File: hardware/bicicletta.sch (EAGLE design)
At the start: 2 parts

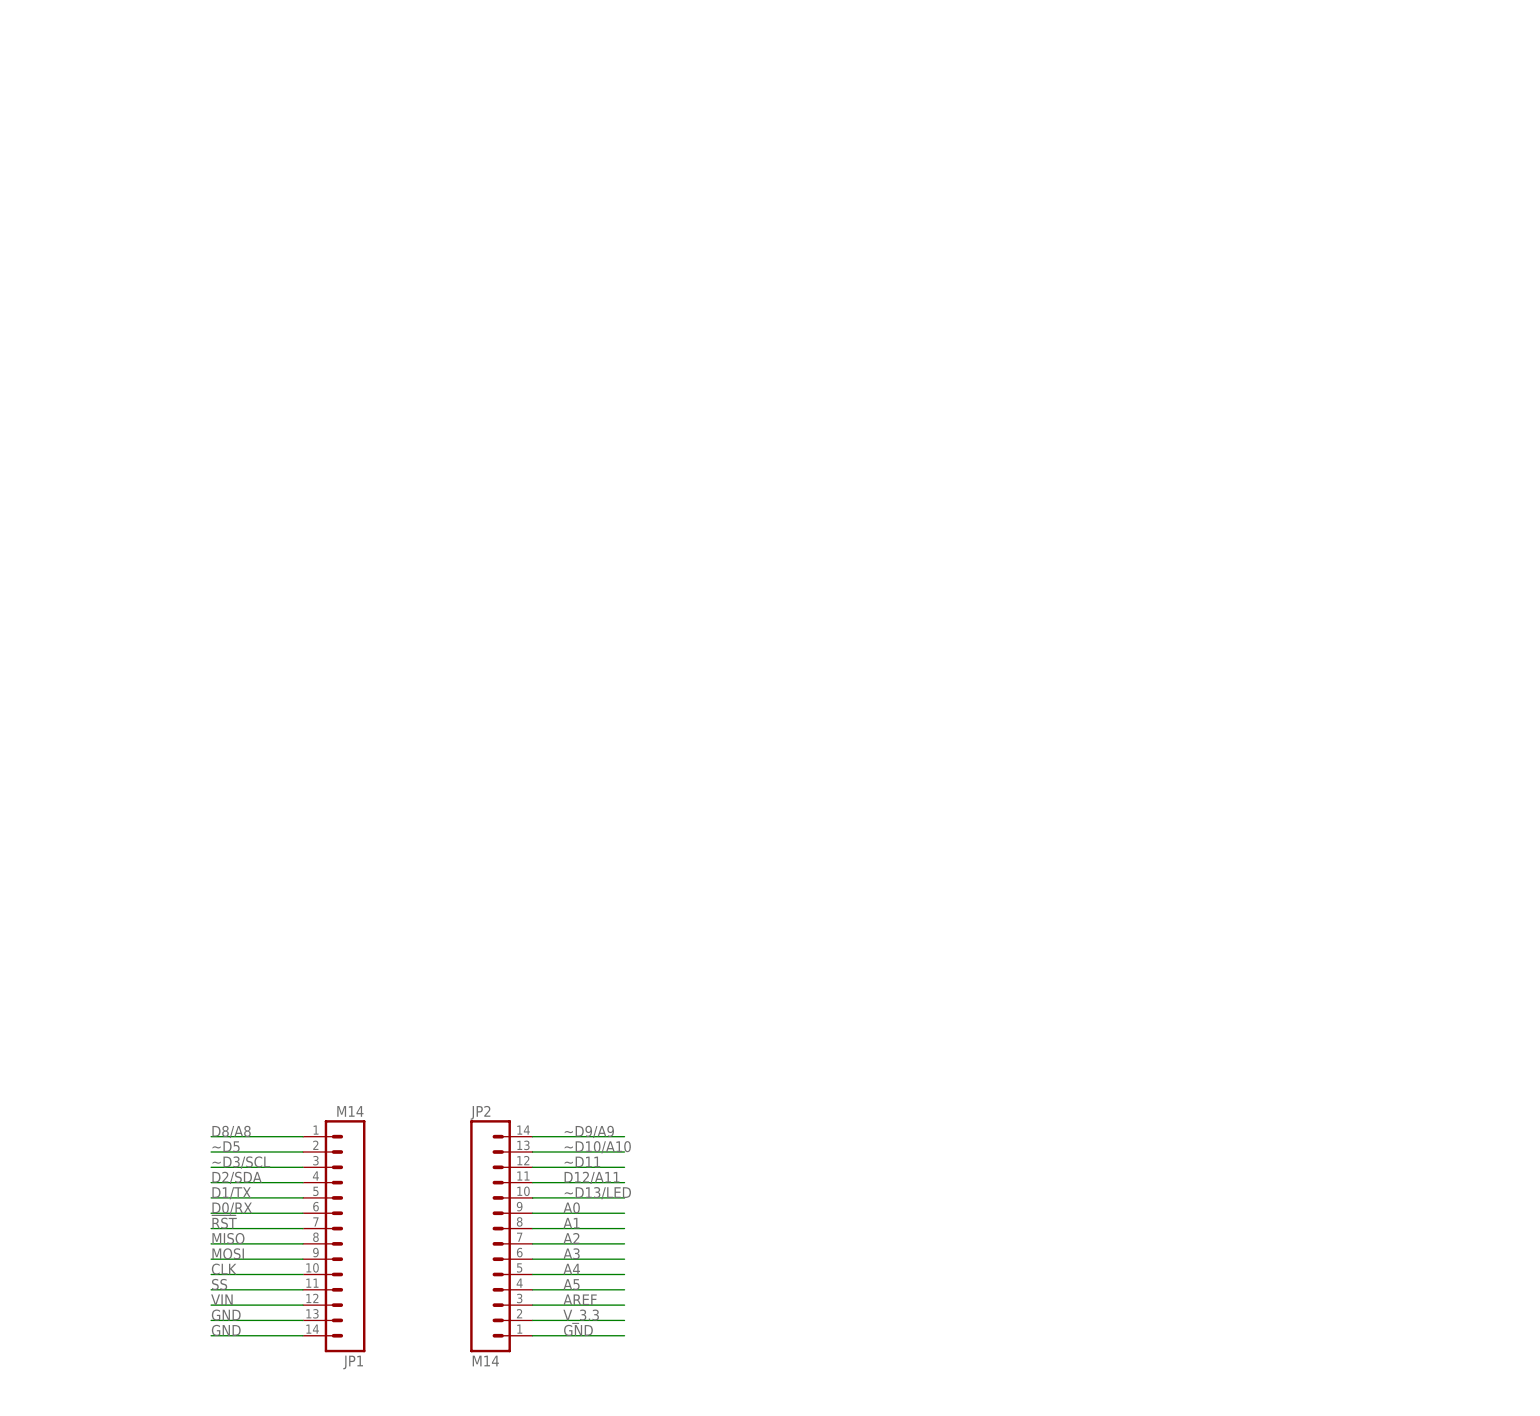
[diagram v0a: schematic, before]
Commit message: Switching regulator is set up in schematic.
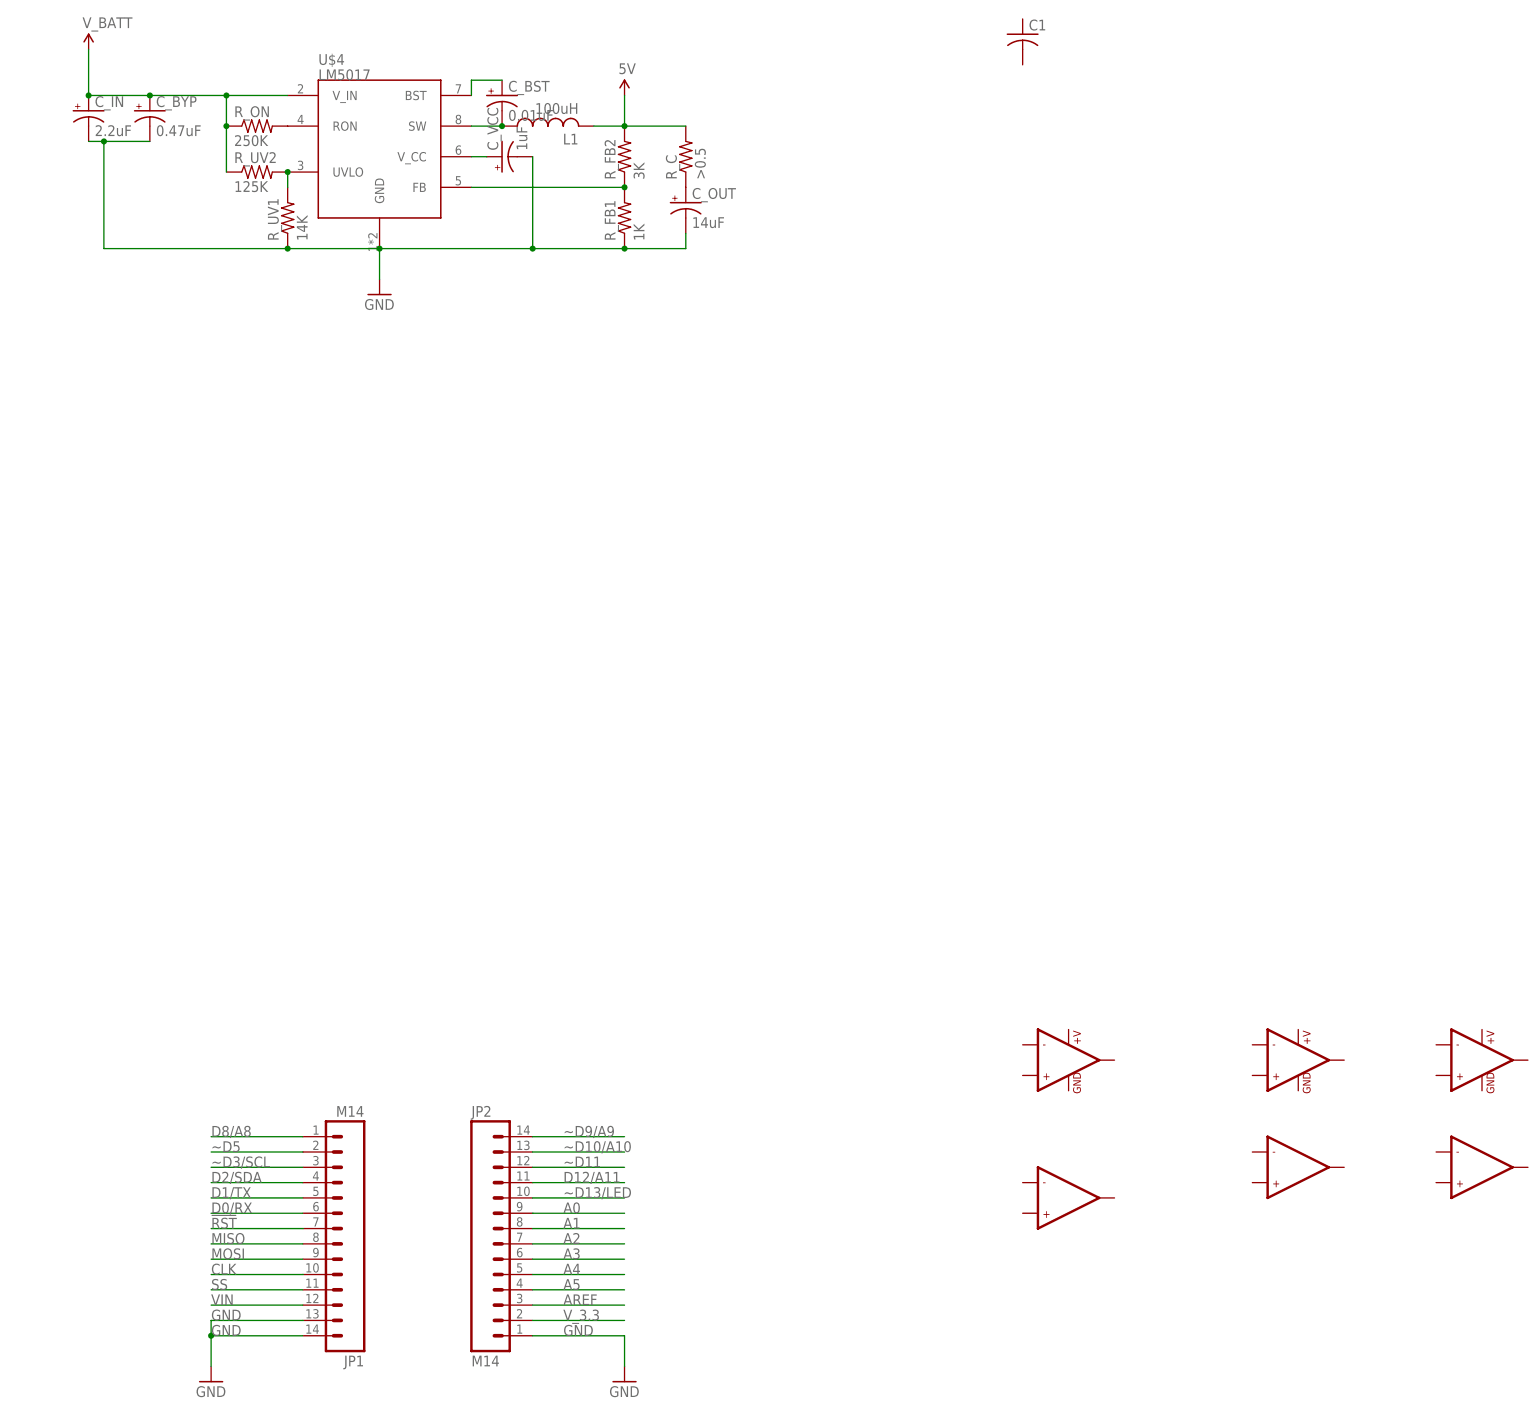
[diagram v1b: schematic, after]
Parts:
- added C1: (no value), rcl:C-USC0805
- added C_BST: 0.01uF, rcl:CPOL-USUD-5X5,8
- added C_BYP: 0.47uF, rcl:CPOL-USUD-5X5,8
- added C_IN: 2.2uF, rcl:CPOL-USUD-5X5,8
- added C_OUT: 14uF, rcl:CPOL-USUD-5X5,8
- added C_VCC: 1uF, rcl:CPOL-USUD-5X5,8
- added L1: 100uH, rcl:L-USL1812
- added R_C: >0.5, rcl:R-US_M0805
- added R_FB1: 1K, rcl:R-US_M0805
- added R_FB2: 3K, rcl:R-US_M0805
- added R_ON: 250K, rcl:R-US_M0805
- added R_UV1: 14K, rcl:R-US_M0805
- added R_UV2: 125K, rcl:R-US_M0805
- added U$1, U$2, U$3: LMV358, SparkFun-AnalogIC:LMV358
- added U$4: LM5017, Railstars:LM5017
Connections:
- new net 1.8V: C_BYP.+, C_IN.+, R_ON.1, R_UV2.1, U$4.V_IN
- new net 5V: L1.2, R_C.2, R_FB2.2
- new net N$1: R_ON.2, U$4.RON
- new net N$2: R_FB1.2, R_FB2.1, U$4.FB
- new net N$3: R_UV1.2, R_UV2.2, U$4.UVLO
- new net N$4: C_VCC.+, U$4.V_CC
- new net N$5: C_BST.-, L1.1, U$4.SW
- new net N$6: C_BST.+, U$4.BST
- new net N$7: C_OUT.+, R_C.1
- net GND: now also C_BYP.-, C_IN.-, C_OUT.-, C_VCC.-, R_FB1.1, R_UV1.1, U$4.GND

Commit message: Added 3.3V LDO regulator
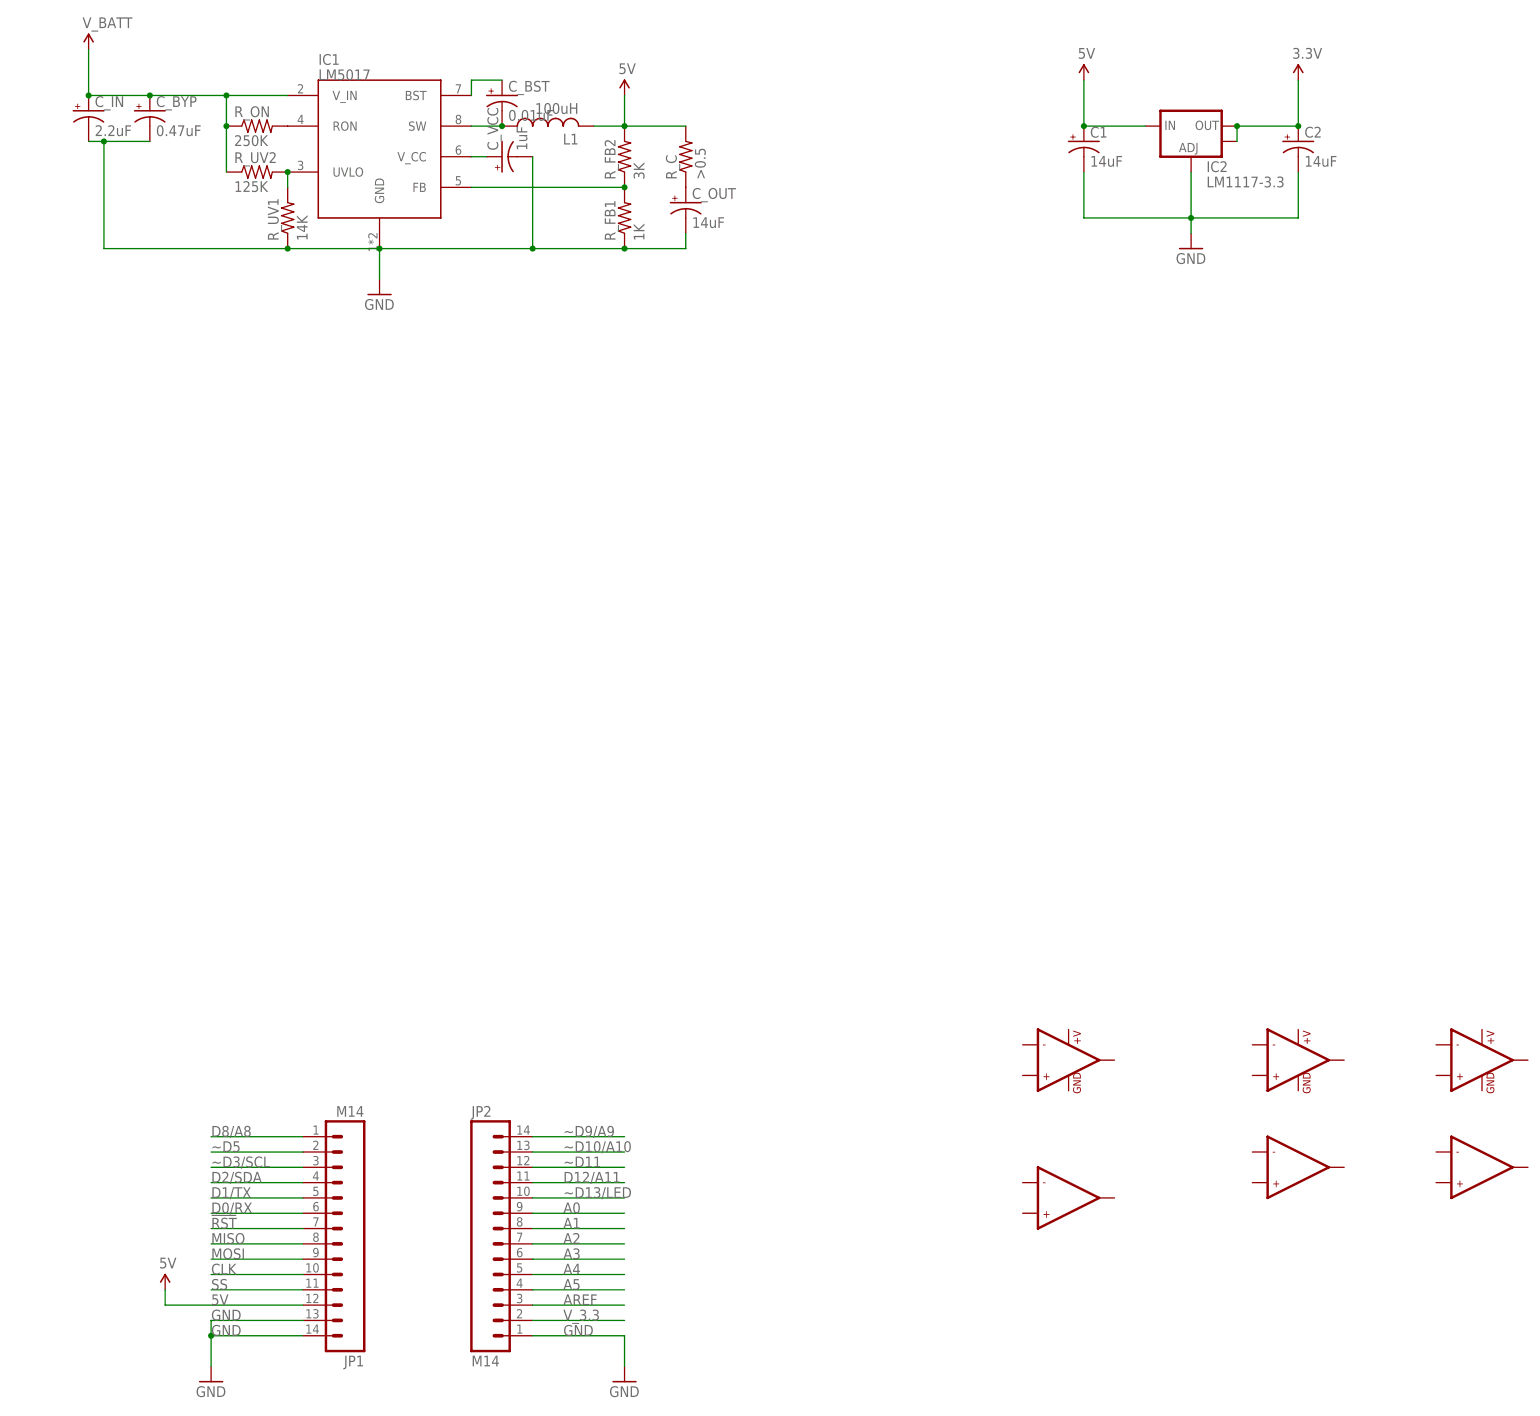
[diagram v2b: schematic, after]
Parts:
- added C2: 14uF, rcl:CPOL-USUD-5X5,8
- added IC2: LM1117-3.3, SparkFun-PowerIC:V_REG_LM1117SOT223
- C1: value (none) -> 14uF; device rcl:C-USC0805 -> rcl:CPOL-USUD-5X5,8
- renumbered U$4 to IC1
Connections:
- removed net VIN: JP1.12
- new net 3.3V: C2.+, IC2.OUT, IC2.OUT@1
- net 5V: now also C1.+, IC2.IN, JP1.12
- net GND: now also C1.-, C2.-, IC2.ADJ
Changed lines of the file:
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@@
 <part name="U$2" library="SparkFun-AnalogIC" deviceset="LMV358" device=""/>
 <part name="U$3" library="SparkFun-AnalogIC" deviceset="LMV358" device=""/>
-<part name="U$4" library="Railstars" deviceset="LM5017" device=""/>
+<part name="IC1" library="Railstars" deviceset="LM5017" device=""/>
 <part name="U$5" library="SparkFun-Aesthetics" deviceset="5V" device=""/>
 <part name="U$6" library="SparkFun-Aesthetics" deviceset="V_BATT" device=""/>
@@
 <part name="GND3" library="SparkFun-Aesthetics" deviceset="GND" device=""/>
 <part name="R_ON" library="rcl" deviceset="R-US_" device="M0805" value="250K"/>
-<part name="C1" library="rcl" deviceset="C-US" device="C0805"/>
 <part name="R_FB2" library="rcl" deviceset="R-US_" device="M0805" value="3K"/>
 <part name="R_FB1" library="rcl" deviceset="R-US_" device="M0805" value="1K"/>
@@
 <part name="L1" library="rcl" deviceset="L-US" device="L1812" value="100uH"/>
 <part name="R_C" library="rcl" deviceset="R-US_" device="M0805" value="&gt;0.5"/>
+<part name="U$7" library="SparkFun-Aesthetics" deviceset="5V" device=""/>
+<part name="IC2" library="SparkFun-PowerIC" deviceset="V_REG_LM1117" device="SOT223" value="LM1117-3.3"/>
+<part name="U$8" library="SparkFun-Aesthetics" deviceset="5V" device=""/>
+<part name="GND4" library="SparkFun-Aesthetics" deviceset="GND" device=""/>
+<part name="P+1" library="SparkFun-Aesthetics" deviceset="3.3V" device=""/>
+<part name="C1" library="rcl" deviceset="CPOL-US" device="UD-5X5,8" value="14uF"/>
+<part name="C2" library="rcl" deviceset="CPOL-US" device="UD-5X5,8" value="14uF"/>
 </parts>
 <sheets>
@@
 <instance part="U$3" gate="G$1" x="238.76" y="83.82"/>
 <instance part="U$3" gate="G$2" x="238.76" y="66.04"/>
-<instance part="U$4" gate="G$1" x="66.04" y="210.82"/>
+<instance part="IC1" gate="G$1" x="66.04" y="210.82"/>
 <instance part="U$5" gate="G$1" x="96.52" y="243.84"/>
 <instance part="U$6" gate="G$1" x="7.62" y="251.46"/>
@@
 <instance part="GND3" gate="1" x="27.94" y="30.48"/>
 <instance part="R_ON" gate="G$1" x="35.56" y="238.76"/>
-<instance part="C1" gate="G$1" x="162.56" y="254"/>
 <instance part="R_FB2" gate="G$1" x="96.52" y="233.68" rot="R90"/>
 <instance part="R_FB1" gate="G$1" x="96.52" y="223.52" rot="R90"/>
@@
 <instance part="L1" gate="G$1" x="83.82" y="238.76" rot="R90"/>
 <instance part="R_C" gate="G$1" x="106.68" y="233.68" rot="R90"/>
+<instance part="U$7" gate="G$1" x="20.32" y="45.72"/>
+<instance part="IC2" gate="G$1" x="190.5" y="238.76"/>
+<instance part="U$8" gate="G$1" x="172.72" y="246.38"/>
+<instance part="GND4" gate="1" x="190.5" y="218.44"/>
+<instance part="P+1" gate="G$1" x="208.28" y="246.38"/>
+<instance part="C1" gate="G$1" x="172.72" y="236.22"/>
+<instance part="C2" gate="G$1" x="208.28" y="236.22"/>
 </instances>
 <busses>
@@
 <wire x1="43.18" y1="45.72" x2="27.94" y2="45.72" width="0.1524" layer="91"/>
 <label x="27.94" y="45.72" size="1.778" layer="95"/>
-</segment>
-</net>
-<net name="VIN" class="0">
-<segment>
-<pinref part="JP1" gate="G$1" pin="12"/>
-<wire x1="43.18" y1="43.18" x2="27.94" y2="43.18" width="0.1524" layer="91"/>
-<label x="27.94" y="43.18" size="1.778" layer="95"/>
 </segment>
 </net>
@@
 </segment>
 <segment>
-<pinref part="U$4" gate="G$1" pin="GND"/>
+<pinref part="IC1" gate="G$1" pin="GND"/>
 <pinref part="GND1" gate="1" pin="GND"/>
 <wire x1="55.88" y1="218.44" x2="55.88" y2="213.36" width="0.1524" layer="91"/>
@@
 <junction x="96.52" y="218.44"/>
 </segment>
+<segment>
+<pinref part="IC2" gate="G$1" pin="ADJ"/>
+<pinref part="GND4" gate="1" pin="GND"/>
+<wire x1="190.5" y1="231.14" x2="190.5" y2="223.52" width="0.1524" layer="91"/>
+<pinref part="C2" gate="G$1" pin="-"/>
+<wire x1="190.5" y1="223.52" x2="190.5" y2="220.98" width="0.1524" layer="91"/>
+<wire x1="208.28" y1="231.14" x2="208.28" y2="223.52" width="0.1524" layer="91"/>
+<wire x1="208.28" y1="223.52" x2="190.5" y2="223.52" width="0.1524" layer="91"/>
+<pinref part="C1" gate="G$1" pin="-"/>
+<wire x1="172.72" y1="231.14" x2="172.72" y2="223.52" width="0.1524" layer="91"/>
+<wire x1="172.72" y1="223.52" x2="190.5" y2="223.52" width="0.1524" layer="91"/>
+<junction x="190.5" y="223.52"/>
+</segment>
 </net>
 <net name="~D9/A9" class="0">
@@
 <pinref part="U$6" gate="G$1" pin="1.8V"/>
 <wire x1="7.62" y1="251.46" x2="7.62" y2="243.84" width="0.1524" layer="91"/>
-<pinref part="U$4" gate="G$1" pin="V_IN"/>
+<pinref part="IC1" gate="G$1" pin="V_IN"/>
 <wire x1="7.62" y1="243.84" x2="17.78" y2="243.84" width="0.1524" layer="91"/>
 <wire x1="17.78" y1="243.84" x2="30.48" y2="243.84" width="0.1524" layer="91"/>
@@
 <wire x1="96.52" y1="238.76" x2="106.68" y2="238.76" width="0.1524" layer="91"/>
 </segment>
+<segment>
+<pinref part="JP1" gate="G$1" pin="12"/>
+<wire x1="43.18" y1="43.18" x2="20.32" y2="43.18" width="0.1524" layer="91"/>
+<label x="27.94" y="43.18" size="1.778" layer="95"/>
+<pinref part="U$7" gate="G$1" pin="5V"/>
+<wire x1="20.32" y1="43.18" x2="20.32" y2="45.72" width="0.1524" layer="91"/>
+</segment>
+<segment>
+<pinref part="IC2" gate="G$1" pin="IN"/>
+<pinref part="U$8" gate="G$1" pin="5V"/>
+<wire x1="182.88" y1="238.76" x2="172.72" y2="238.76" width="0.1524" layer="91"/>
+<wire x1="172.72" y1="238.76" x2="172.72" y2="246.38" width="0.1524" layer="91"/>
+<pinref part="C1" gate="G$1" pin="+"/>
+<junction x="172.72" y="238.76"/>
+</segment>
 </net>
 <net name="N$1" class="0">
 <segment>
-<pinref part="U$4" gate="G$1" pin="RON"/>
+<pinref part="IC1" gate="G$1" pin="RON"/>
 <pinref part="R_ON" gate="G$1" pin="2"/>
 </segment>
@@
 <pinref part="R_FB2" gate="G$1" pin="1"/>
 <pinref part="R_FB1" gate="G$1" pin="2"/>
-<pinref part="U$4" gate="G$1" pin="FB"/>
+<pinref part="IC1" gate="G$1" pin="FB"/>
 <wire x1="71.12" y1="228.6" x2="96.52" y2="228.6" width="0.1524" layer="91"/>
 <junction x="96.52" y="228.6"/>
@@
 <net name="N$3" class="0">
 <segment>
-<pinref part="U$4" gate="G$1" pin="UVLO"/>
+<pinref part="IC1" gate="G$1" pin="UVLO"/>
 <pinref part="R_UV2" gate="G$1" pin="2"/>
 <pinref part="R_UV1" gate="G$1" pin="2"/>
@@
 <net name="N$4" class="0">
 <segment>
-<pinref part="U$4" gate="G$1" pin="V_CC"/>
+<pinref part="IC1" gate="G$1" pin="V_CC"/>
 <wire x1="71.12" y1="233.68" x2="73.66" y2="233.68" width="0.1524" layer="91"/>
 <pinref part="C_VCC" gate="G$1" pin="+"/>
@@
 <net name="N$5" class="0">
 <segment>
-<pinref part="U$4" gate="G$1" pin="SW"/>
+<pinref part="IC1" gate="G$1" pin="SW"/>
 <pinref part="L1" gate="G$1" pin="1"/>
 <wire x1="71.12" y1="238.76" x2="76.2" y2="238.76" width="0.1524" layer="91"/>
@@
 <net name="N$6" class="0">
 <segment>
-<pinref part="U$4" gate="G$1" pin="BST"/>
+<pinref part="IC1" gate="G$1" pin="BST"/>
 <pinref part="C_BST" gate="G$1" pin="+"/>
 <wire x1="76.2" y1="246.38" x2="71.12" y2="246.38" width="0.1524" layer="91"/>
@@
 </segment>
 </net>
+<net name="3.3V" class="0">
+<segment>
+<pinref part="IC2" gate="G$1" pin="OUT@1"/>
+<pinref part="IC2" gate="G$1" pin="OUT"/>
+<wire x1="198.12" y1="236.22" x2="198.12" y2="238.76" width="0.1524" layer="91"/>
+<wire x1="198.12" y1="238.76" x2="208.28" y2="238.76" width="0.1524" layer="91"/>
+<wire x1="208.28" y1="238.76" x2="208.28" y2="246.38" width="0.1524" layer="91"/>
+<pinref part="P+1" gate="G$1" pin="3.3V"/>
+<pinref part="C2" gate="G$1" pin="+"/>
+<junction x="208.28" y="238.76"/>
+<junction x="198.12" y="238.76"/>
+</segment>
+</net>
